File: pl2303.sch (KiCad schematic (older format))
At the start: 24 parts, among them P2 USB_OTG, U2 PL2303, Y1 CRYSTAL

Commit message: Питание и LM2596
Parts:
- C19, C4: footprint Capacitors_SMD:C_0603_HandSoldering -> Capacitors_SMD:C_0805
- R1, R12, R13, R2, R7, R8: footprint Resistors_ThroughHole:Resistor_Horizontal_RM10mm -> Resistors_SMD:R_0805
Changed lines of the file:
@@
 $EndComp
 $Comp
-L GND #PWR023
+L GND #PWR022
 U 1 1 5705278D
 P 9200 4000
-F 0 "#PWR023" H 9200 3750 50  0001 C CNN
+F 0 "#PWR022" H 9200 3750 50  0001 C CNN
 F 1 "GND" H 9200 3850 50  0000 C CNN
 F 2 "" H 9200 4000 50  0000 C CNN
@@
 $EndComp
 $Comp
-L GND #PWR024
+L GND #PWR023
 U 1 1 570529E3
 P 8500 5700
-F 0 "#PWR024" H 8500 5450 50  0001 C CNN
+F 0 "#PWR023" H 8500 5450 50  0001 C CNN
 F 1 "GND" H 8500 5550 50  0000 C CNN
 F 2 "" H 8500 5700 50  0000 C CNN
@@
 F 0 "R7" V 3180 5200 50  0000 C CNN
 F 1 "220-470" V 3100 5200 50  0000 C CNN
-F 2 "Resistors_ThroughHole:Resistor_Horizontal_RM10mm" V 3030 5200 50  0001 C CNN
+F 2 "Resistors_SMD:R_0805" V 3030 5200 50  0001 C CNN
 F 3 "" H 3100 5200 50  0000 C CNN
 	1    3100 5200
@@
 $EndComp
 $Comp
-L GND #PWR025
+L GND #PWR024
 U 1 1 570620C0
 P 2950 5500
-F 0 "#PWR025" H 2950 5250 50  0001 C CNN
+F 0 "#PWR024" H 2950 5250 50  0001 C CNN
 F 1 "GND" H 2950 5350 50  0000 C CNN
 F 2 "" H 2950 5500 50  0000 C CNN
@@
 F 0 "C19" H 1325 3600 50  0000 L CNN
 F 1 "27pF" H 1325 3400 50  0000 L CNN
-F 2 "Capacitors_SMD:C_0603_HandSoldering" H 1338 3350 50  0001 C CNN
+F 2 "Capacitors_SMD:C_0805" H 1338 3350 50  0001 C CNN
 F 3 "" H 1300 3500 50  0000 C CNN
 	1    1300 3500
@@
 F 0 "C4" H 625 3600 50  0000 L CNN
 F 1 "27pF" H 625 3400 50  0000 L CNN
-F 2 "Capacitors_SMD:C_0603_HandSoldering" H 638 3350 50  0001 C CNN
+F 2 "Capacitors_SMD:C_0805" H 638 3350 50  0001 C CNN
 F 3 "" H 600 3500 50  0000 C CNN
 	1    600  3500
@@
 $EndComp
 $Comp
-L GND #PWR026
+L GND #PWR025
 U 1 1 570D14D2
 P 950 3800
-F 0 "#PWR026" H 950 3550 50  0001 C CNN
+F 0 "#PWR025" H 950 3550 50  0001 C CNN
 F 1 "GND" H 950 3650 50  0000 C CNN
 F 2 "" H 950 3800 50  0000 C CNN
@@
 F 0 "R1" V 2880 5200 50  0000 C CNN
 F 1 "220-470" V 2800 5200 50  0000 C CNN
-F 2 "Resistors_ThroughHole:Resistor_Horizontal_RM10mm" V 2730 5200 50  0001 C CNN
+F 2 "Resistors_SMD:R_0805" V 2730 5200 50  0001 C CNN
 F 3 "" H 2800 5200 50  0000 C CNN
 	1    2800 5200
@@
 NoConn ~ 3550 3700
 $Comp
-L GND #PWR027
+L GND #PWR026
 U 1 1 570D2EBB
 P 2450 5100
-F 0 "#PWR027" H 2450 4850 50  0001 C CNN
+F 0 "#PWR026" H 2450 4850 50  0001 C CNN
 F 1 "GND" H 2450 4950 50  0000 C CNN
 F 2 "" H 2450 5100 50  0000 C CNN
@@
 F 0 "R2" V 4080 2900 50  0000 C CNN
 F 1 "220" V 4000 2900 50  0000 C CNN
-F 2 "Resistors_ThroughHole:Resistor_Horizontal_RM10mm" V 3930 2900 50  0001 C CNN
+F 2 "Resistors_SMD:R_0805" V 3930 2900 50  0001 C CNN
 F 3 "" H 4000 2900 50  0000 C CNN
 	1    4000 2900
@@
 $EndComp
 $Comp
-L GND #PWR028
+L GND #PWR027
 U 1 1 570D2F71
 P 4850 3050
-F 0 "#PWR028" H 4850 2800 50  0001 C CNN
+F 0 "#PWR027" H 4850 2800 50  0001 C CNN
 F 1 "GND" H 4850 2900 50  0000 C CNN
 F 2 "" H 4850 3050 50  0000 C CNN
@@
 F 0 "R8" V 4430 2800 50  0000 C CNN
 F 1 "220" V 4350 2800 50  0000 C CNN
-F 2 "Resistors_ThroughHole:Resistor_Horizontal_RM10mm" V 4280 2800 50  0001 C CNN
+F 2 "Resistors_SMD:R_0805" V 4280 2800 50  0001 C CNN
 F 3 "" H 4350 2800 50  0000 C CNN
 	1    4350 2800
@@
 $EndComp
 $Comp
-L +3.3V #PWR029
+L +3.3V #PWR028
 U 1 1 570D3933
 P 9200 2900
-F 0 "#PWR029" H 9200 2750 50  0001 C CNN
+F 0 "#PWR028" H 9200 2750 50  0001 C CNN
 F 1 "+3.3V" H 9200 3040 50  0000 C CNN
 F 2 "" H 9200 2900 50  0000 C CNN
@@
 $EndComp
 $Comp
-L +5V #PWR030
+L +5V #PWR029
 U 1 1 5717E4F4
 P 8300 1100
-F 0 "#PWR030" H 8300 950 50  0001 C CNN
+F 0 "#PWR029" H 8300 950 50  0001 C CNN
 F 1 "+5V" H 8300 1240 50  0000 C CNN
 F 2 "" H 8300 1100 50  0000 C CNN
@@
 $EndComp
 $Comp
-L GND #PWR031
+L GND #PWR030
 U 1 1 5717E503
 P 8300 2150
-F 0 "#PWR031" H 8300 1900 50  0001 C CNN
+F 0 "#PWR030" H 8300 1900 50  0001 C CNN
 F 1 "GND" H 8300 2000 50  0000 C CNN
 F 2 "" H 8300 2150 50  0000 C CNN
@@
 $EndComp
 $Comp
-L +5V #PWR032
+L +5V #PWR031
 U 1 1 5717F490
 P 2450 1450
-F 0 "#PWR032" H 2450 1300 50  0001 C CNN
+F 0 "#PWR031" H 2450 1300 50  0001 C CNN
 F 1 "+5V" H 2450 1590 50  0000 C CNN
 F 2 "" H 2450 1450 50  0000 C CNN
@@
 F 0 "R13" V 3980 3600 50  0000 C CNN
 F 1 "470" V 3900 3600 50  0000 C CNN
-F 2 "Resistors_ThroughHole:Resistor_Horizontal_RM10mm" V 3830 3600 50  0001 C CNN
+F 2 "Resistors_SMD:R_0805" V 3830 3600 50  0001 C CNN
 F 3 "" H 3900 3600 50  0000 C CNN
 	1    3900 3600
@@
 F 0 "R12" V 3880 3900 50  0000 C CNN
 F 1 "470" V 3800 3900 50  0000 C CNN
-F 2 "Resistors_ThroughHole:Resistor_Horizontal_RM10mm" V 3730 3900 50  0001 C CNN
+F 2 "Resistors_SMD:R_0805" V 3730 3900 50  0001 C CNN
 F 3 "" H 3800 3900 50  0000 C CNN
 	1    3800 3900
@@
 	2750 1450 2750 2300
 $Comp
-L +3.3V #PWR033
+L +3.3V #PWR032
 U 1 1 571E53D2
 P 2750 1450
-F 0 "#PWR033" H 2750 1300 50  0001 C CNN
+F 0 "#PWR032" H 2750 1300 50  0001 C CNN
 F 1 "+3.3V" H 2750 1590 50  0000 C CNN
 F 2 "" H 2750 1450 50  0000 C CNN
@@
 $EndComp
 $Comp
-L +3.3V #PWR034
+L +3.3V #PWR033
 U 1 1 571E5683
 P 7700 5350
-F 0 "#PWR034" H 7700 5200 50  0001 C CNN
+F 0 "#PWR033" H 7700 5200 50  0001 C CNN
 F 1 "+3.3V" H 7700 5490 50  0000 C CNN
 F 2 "" H 7700 5350 50  0000 C CNN
@@
 	8500 5000 8500 4400
 $Comp
-L +5V #PWR035
+L +5V #PWR034
 U 1 1 571E81DD
 P 8500 4400
-F 0 "#PWR035" H 8500 4250 50  0001 C CNN
+F 0 "#PWR034" H 8500 4250 50  0001 C CNN
 F 1 "+5V" H 8500 4540 50  0000 C CNN
 F 2 "" H 8500 4400 50  0000 C CNN
@@
 $EndComp
 $Comp
-L +5V #PWR036
+L +5V #PWR035
 U 1 1 571E851C
 P 4600 1700
-F 0 "#PWR036" H 4600 1550 50  0001 C CNN
+F 0 "#PWR035" H 4600 1550 50  0001 C CNN
 F 1 "+5V" H 4600 1840 50  0000 C CNN
 F 2 "" H 4600 1700 50  0000 C CNN

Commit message: Готовая плата версия_1
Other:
- note added: "17"
- note added: "20"
- note added: "24"
- note added: "4"
- note added: "8"
- moved on the sheet: C16, C3, C5, C6
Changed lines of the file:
@@
 LIBS:Pulse_Module-rescue
 LIBS:conn3
-LIBS:pl2303
 LIBS:power
 LIBS:device
@@
 Text HLabel 4400 4150 2    60   Input ~ 0
 RXD
-NoConn ~ 9050 5500
 NoConn ~ 3550 3100
 $Comp
@@
 L C C3
 U 1 1 5717E48A
-P 7900 1650
-F 0 "C3" H 7925 1750 50  0000 L CNN
-F 1 "0.1uF" H 7925 1550 50  0000 L CNN
-F 2 "Capacitors_SMD:C_0805" H 7938 1500 50  0001 C CNN
-F 3 "" H 7900 1650 50  0000 C CNN
-	1    7900 1650
+P 795 1440
+F 0 "C3" H 820 1540 50  0000 L CNN
+F 1 "0.1uF" H 820 1340 50  0000 L CNN
+F 2 "Capacitors_SMD:C_0805" H 833 1290 50  0001 C CNN
+F 3 "" H 795 1440 50  0000 C CNN
+	1    795  1440
 	-1   0    0    1
 $EndComp
@@
 L C C5
 U 1 1 5717E499
-P 8300 1650
-F 0 "C5" H 8325 1750 50  0000 L CNN
-F 1 "0.1uF" H 8325 1550 50  0000 L CNN
-F 2 "Capacitors_SMD:C_0805" H 8338 1500 50  0001 C CNN
-F 3 "" H 8300 1650 50  0000 C CNN
-	1    8300 1650
+P 1195 1440
+F 0 "C5" H 1220 1540 50  0000 L CNN
+F 1 "0.1uF" H 1220 1340 50  0000 L CNN
+F 2 "Capacitors_SMD:C_0805" H 1233 1290 50  0001 C CNN
+F 3 "" H 1195 1440 50  0000 C CNN
+	1    1195 1440
 	-1   0    0    1
 $EndComp
@@
 L C C6
 U 1 1 5717E4A8
-P 8700 1650
-F 0 "C6" H 8725 1750 50  0000 L CNN
-F 1 "0.1uF" H 8725 1550 50  0000 L CNN
-F 2 "Capacitors_SMD:C_0805" H 8738 1500 50  0001 C CNN
-F 3 "" H 8700 1650 50  0000 C CNN
-	1    8700 1650
+P 1595 1440
+F 0 "C6" H 1620 1540 50  0000 L CNN
+F 1 "0.1uF" H 1620 1340 50  0000 L CNN
+F 2 "Capacitors_SMD:C_0805" H 1633 1290 50  0001 C CNN
+F 3 "" H 1595 1440 50  0000 C CNN
+	1    1595 1440
 	-1   0    0    1
 $EndComp
@@
 L +5V #PWR029
 U 1 1 5717E4F4
-P 8300 1100
-F 0 "#PWR029" H 8300 950 50  0001 C CNN
-F 1 "+5V" H 8300 1240 50  0000 C CNN
-F 2 "" H 8300 1100 50  0000 C CNN
-F 3 "" H 8300 1100 50  0000 C CNN
-	1    8300 1100
+P 1195 890
+F 0 "#PWR029" H 1195 740 50  0001 C CNN
+F 1 "+5V" H 1195 1030 50  0000 C CNN
+F 2 "" H 1195 890 50  0000 C CNN
+F 3 "" H 1195 890 50  0000 C CNN
+	1    1195 890
 	1    0    0    -1
 $EndComp
@@
 L GND #PWR030
 U 1 1 5717E503
-P 8300 2150
-F 0 "#PWR030" H 8300 1900 50  0001 C CNN
-F 1 "GND" H 8300 2000 50  0000 C CNN
-F 2 "" H 8300 2150 50  0000 C CNN
-F 3 "" H 8300 2150 50  0000 C CNN
-	1    8300 2150
+P 1195 1940
+F 0 "#PWR030" H 1195 1690 50  0001 C CNN
+F 1 "GND" H 1195 1790 50  0000 C CNN
+F 2 "" H 1195 1940 50  0000 C CNN
+F 3 "" H 1195 1940 50  0000 C CNN
+	1    1195 1940
 	1    0    0    -1
 $EndComp
@@
 	2550 1650 2550 2300
 Wire Wire Line
-	7900 1800 7900 1950
-Wire Wire Line
-	7900 1950 9050 1950
-Wire Wire Line
-	8700 1950 8700 1800
-Wire Wire Line
-	8700 1350 8700 1500
-Wire Wire Line
-	7900 1350 7900 1500
-Wire Wire Line
-	7900 1350 9050 1350
-Wire Wire Line
-	8300 1100 8300 1500
-Connection ~ 8300 1350
-Wire Wire Line
-	8300 1800 8300 2150
-Connection ~ 8300 1950
+	795  1590 795  1740
+Wire Wire Line
+	795  1740 1945 1740
+Wire Wire Line
+	1595 1740 1595 1590
+Wire Wire Line
+	1595 1140 1595 1290
+Wire Wire Line
+	795  1140 795  1290
+Wire Wire Line
+	795  1140 1945 1140
+Wire Wire Line
+	1195 890  1195 1290
+Connection ~ 1195 1140
+Wire Wire Line
+	1195 1590 1195 1940
+Connection ~ 1195 1740
 Wire Wire Line
 	2350 2300 2350 1650
@@
 	7700 6300 7700 6000
 Wire Wire Line
-	7700 5700 7700 5350
-Wire Wire Line
 	4400 4150 4200 4150
 Connection ~ 4200 4150
@@
 Wire Wire Line
 	2750 1450 2750 2300
-$Comp
-L +3.3V #PWR032
-U 1 1 571E53D2
-P 2750 1450
-F 0 "#PWR032" H 2750 1300 50  0001 C CNN
-F 1 "+3.3V" H 2750 1590 50  0000 C CNN
-F 2 "" H 2750 1450 50  0000 C CNN
-F 3 "" H 2750 1450 50  0000 C CNN
-	1    2750 1450
-	1    0    0    -1
-$EndComp
-$Comp
-L +3.3V #PWR033
-U 1 1 571E5683
-P 7700 5350
-F 0 "#PWR033" H 7700 5200 50  0001 C CNN
-F 1 "+3.3V" H 7700 5490 50  0000 C CNN
-F 2 "" H 7700 5350 50  0000 C CNN
-F 3 "" H 7700 5350 50  0000 C CNN
-	1    7700 5350
-	1    0    0    -1
-$EndComp
 $Comp
 L C C15
@@
 	8500 5000 8500 4400
 $Comp
-L +5V #PWR034
+L +5V #PWR032
 U 1 1 571E81DD
 P 8500 4400
-F 0 "#PWR034" H 8500 4250 50  0001 C CNN
+F 0 "#PWR032" H 8500 4250 50  0001 C CNN
 F 1 "+5V" H 8500 4540 50  0000 C CNN
 F 2 "" H 8500 4400 50  0000 C CNN
@@
 $EndComp
 $Comp
-L +5V #PWR035
+L +5V #PWR033
 U 1 1 571E851C
 P 4600 1700
-F 0 "#PWR035" H 4600 1550 50  0001 C CNN
+F 0 "#PWR033" H 4600 1550 50  0001 C CNN
 F 1 "+5V" H 4600 1840 50  0000 C CNN
 F 2 "" H 4600 1700 50  0000 C CNN
@@
 L C C16
 U 1 1 5739D45A
-P 9050 1650
-F 0 "C16" H 9075 1750 50  0000 L CNN
-F 1 "0.1uF" H 9075 1550 50  0000 L CNN
-F 2 "Capacitors_SMD:C_0805" H 9088 1500 50  0001 C CNN
-F 3 "" H 9050 1650 50  0000 C CNN
-	1    9050 1650
-	1    0    0    -1
-$EndComp
-Wire Wire Line
-	9050 1350 9050 1500
-Connection ~ 8700 1350
-Wire Wire Line
-	9050 1950 9050 1800
-Connection ~ 8700 1950
+P 1945 1440
+F 0 "C16" H 1970 1540 50  0000 L CNN
+F 1 "0.1uF" H 1970 1340 50  0000 L CNN
+F 2 "Capacitors_SMD:C_0805" H 1983 1290 50  0001 C CNN
+F 3 "" H 1945 1440 50  0000 C CNN
+	1    1945 1440
+	1    0    0    -1
+$EndComp
+Wire Wire Line
+	1945 1140 1945 1290
+Connection ~ 1595 1140
+Wire Wire Line
+	1945 1740 1945 1590
+Connection ~ 1595 1740
+NoConn ~ 9050 5600
+Wire Wire Line
+	7700 5700 7700 5605
+$Comp
+L +3.3V #PWR034
+U 1 1 574DBF4C
+P 7700 5605
+F 0 "#PWR034" H 7700 5455 50  0001 C CNN
+F 1 "+3.3V" H 7700 5745 50  0000 C CNN
+F 2 "" H 7700 5605 50  0000 C CNN
+F 3 "" H 7700 5605 50  0000 C CNN
+	1    7700 5605
+	1    0    0    -1
+$EndComp
+$Comp
+L +3.3V #PWR035
+U 1 1 574DC8B0
+P 2750 1450
+F 0 "#PWR035" H 2750 1300 50  0001 C CNN
+F 1 "+3.3V" H 2750 1590 50  0000 C CNN
+F 2 "" H 2750 1450 50  0000 C CNN
+F 3 "" H 2750 1450 50  0000 C CNN
+	1    2750 1450
+	1    0    0    -1
+$EndComp
+Text Notes 670  1665 0    60   ~ 0
+4
+Text Notes 1100 1665 0    60   ~ 0
+8
+Text Notes 1435 1675 0    60   ~ 0
+24
+Text Notes 1820 1640 0    60   ~ 0
+20
+Text Notes 8595 3655 0    60   ~ 0
+17
 $EndSCHEMATC

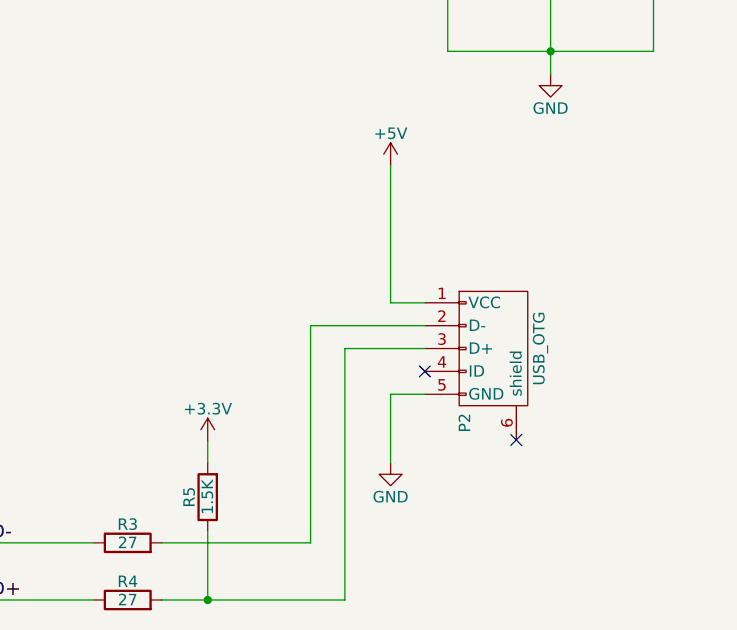
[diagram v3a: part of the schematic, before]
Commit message: подключение питания LMки от USB
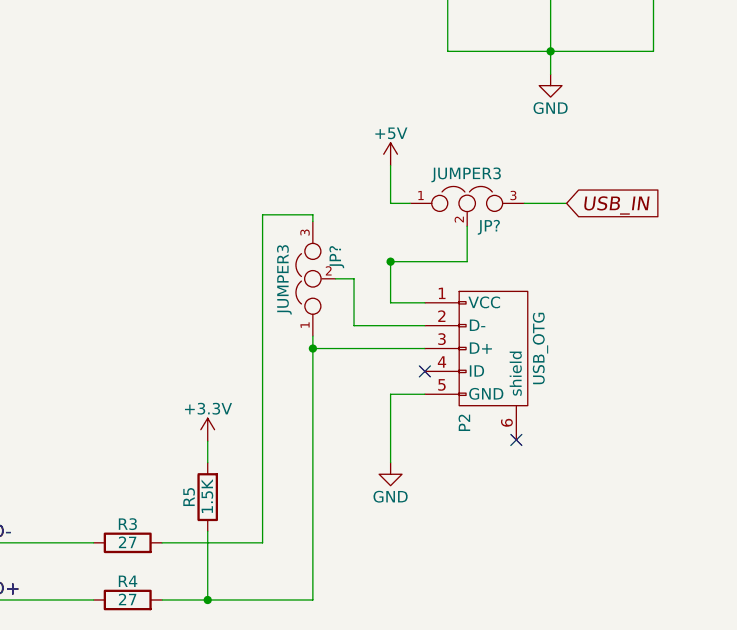
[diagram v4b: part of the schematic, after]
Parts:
- added JP? (x2): JUMPER3, symbol JUMPER3
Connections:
- net +5V: now also JP?.1; no longer P2.1 (VCC)
- net at R3.2: now also JP?.3; no longer P2.2 (D-)
- net at P2.3 (D+), R4.2, R5.1: now also JP?.1
- new net: JP?.2, P2.1 (VCC)
- new net: JP?.2, P2.2 (D-)
- new net USB_IN: JP?.3
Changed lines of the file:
@@
 LIBS:Pulse_Module-rescue
 LIBS:conn3
+LIBS:pl2303
 LIBS:power
 LIBS:device
@@
 Wire Wire Line
 	7200 6300 6750 6300
-Wire Wire Line
-	7500 6050 8150 6050
-Wire Wire Line
-	7500 6300 8300 6300
 Connection ~ 7700 6300
-Wire Wire Line
-	8150 6050 8150 5100
-Wire Wire Line
-	8150 5100 8650 5100
-Wire Wire Line
-	8300 6300 8300 5200
-Wire Wire Line
-	8300 5200 8650 5200
 Wire Wire Line
 	2800 4650 3550 4650
@@
 Wire Wire Line
 	8650 5000 8500 5000
-Wire Wire Line
-	8500 5000 8500 4400
 $Comp
 L +5V #PWR032
@@
 Text Notes 8595 3655 0    60   ~ 0
 17
+Wire Wire Line
+	8160 5200 8650 5200
+Wire Wire Line
+	7940 6050 7500 6050
+Wire Wire Line
+	8160 5145 8160 6300
+Wire Wire Line
+	8160 6300 7500 6300
+Wire Wire Line
+	7940 4615 7940 6050
+$Comp
+L JUMPER3 JP?
+U 1 1 577BDA08
+P 8160 4895
+F 0 "JP?" H 8210 4795 50  0000 L CNN
+F 1 "JUMPER3" H 8160 4995 50  0000 C BNN
+F 2 "" H 8160 4895 50  0000 C CNN
+F 3 "" H 8160 4895 50  0000 C CNN
+	1    8160 4895
+	0    -1   -1   0
+$EndComp
+Wire Wire Line
+	8650 5100 8340 5100
+Wire Wire Line
+	8340 5100 8340 4895
+Wire Wire Line
+	8340 4895 8260 4895
+Connection ~ 8160 5200
+Wire Wire Line
+	8160 4645 8160 4615
+Wire Wire Line
+	8160 4615 7940 4615
+$Comp
+L JUMPER3 JP?
+U 1 1 577BEAFF
+P 8835 4565
+F 0 "JP?" H 8885 4465 50  0000 L CNN
+F 1 "JUMPER3" H 8835 4665 50  0000 C BNN
+F 2 "" H 8835 4565 50  0000 C CNN
+F 3 "" H 8835 4565 50  0000 C CNN
+	1    8835 4565
+	1    0    0    -1
+$EndComp
+Wire Wire Line
+	8500 4820 8835 4820
+Wire Wire Line
+	8835 4820 8835 4665
+Connection ~ 8500 4820
+Wire Wire Line
+	8500 5000 8500 4820
+Wire Wire Line
+	8585 4565 8500 4565
+Wire Wire Line
+	8500 4565 8500 4400
+Wire Wire Line
+	9085 4565 9270 4565
+Text GLabel 9270 4565 2    60   Input Italic 0
+USB_IN
 $EndSCHEMATC
